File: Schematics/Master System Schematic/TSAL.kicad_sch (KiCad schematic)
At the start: 0 parts

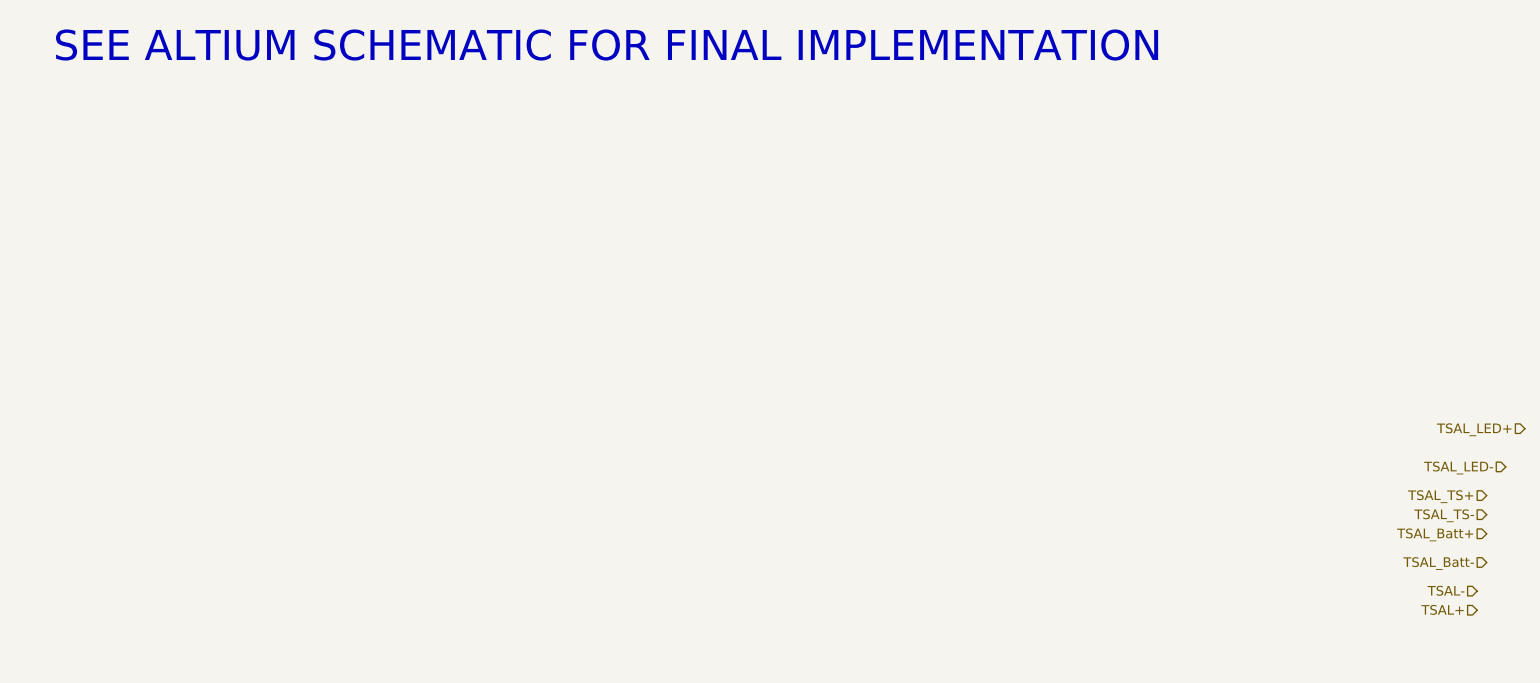
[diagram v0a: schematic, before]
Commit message: Clean up
- Cleaned TSAL
- Added some wire sizes to LV plate @ziptol you need to add remaining wire sizes here
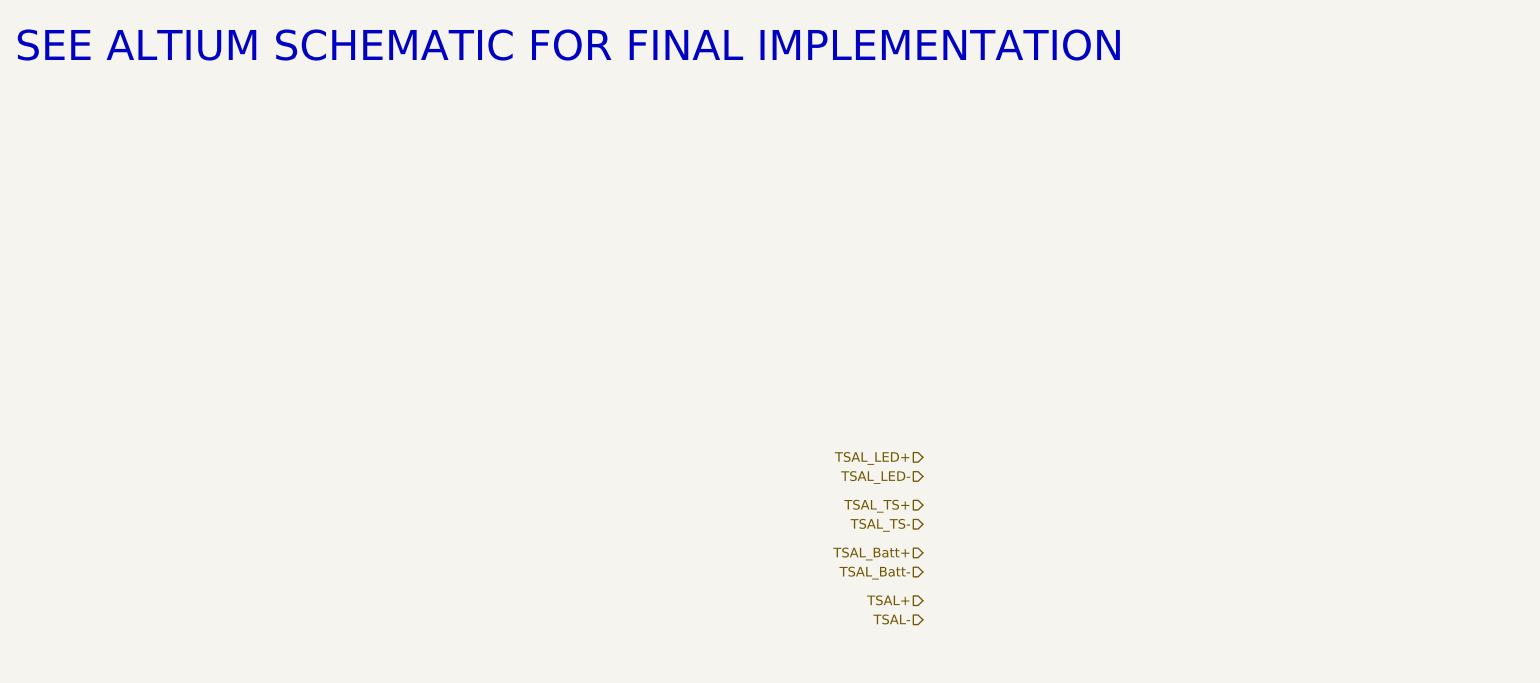
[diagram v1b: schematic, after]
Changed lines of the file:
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@@
 (kicad_sch (version 20211123) (generator eeschema)
-  (paper "A4")
+  (paper "A")
   (title_block
-    (date "2021-11-10")
+    (date "2022-01-29")
+    (rev "0")
     (company "Northeastern Electric Racing")
     (comment 1 "https://github.com/Northeastern-Electric-Racing/NER")
     (comment 2 "For authors and other info, contact Chief Electrical Engineer")
   )
-  (text "SEE ALTIUM SCHEMATIC FOR FINAL IMPLEMENTATION" (at 67.31 33.02 0)
+  (text "SEE ALTIUM SCHEMATIC FOR FINAL IMPLEMENTATION" (at 62.23 33.02 0)
     (effects (font (size 3.9878 3.9878)) (justify left bottom))
   )
-  (hierarchical_label "TSAL-" (shape input) (at 256.54 102.87 180)
+  (hierarchical_label "TSAL-" (shape input) (at 182.88 106.68 180)
     (effects (font (size 1.27 1.27)) (justify right))
   )
-  (hierarchical_label "TSAL_TS-" (shape input) (at 257.81 92.71 180)
+  (hierarchical_label "TSAL_TS-" (shape input) (at 182.88 93.98 180)
     (effects (font (size 1.27 1.27)) (justify right))
   )
-  (hierarchical_label "TSAL_LED+" (shape input) (at 262.89 81.28 180)
+  (hierarchical_label "TSAL_LED+" (shape input) (at 182.88 85.09 180)
     (effects (font (size 1.27 1.27)) (justify right))
   )
-  (hierarchical_label "TSAL_Batt-" (shape input) (at 257.81 99.06 180)
+  (hierarchical_label "TSAL_Batt-" (shape input) (at 182.88 100.33 180)
     (effects (font (size 1.27 1.27)) (justify right))
   )
-  (hierarchical_label "TSAL+" (shape input) (at 256.54 105.41 180)
+  (hierarchical_label "TSAL+" (shape input) (at 182.88 104.14 180)
     (effects (font (size 1.27 1.27)) (justify right))
   )
-  (hierarchical_label "TSAL_LED-" (shape input) (at 260.35 86.36 180)
+  (hierarchical_label "TSAL_LED-" (shape input) (at 182.88 87.63 180)
     (effects (font (size 1.27 1.27)) (justify right))
   )
-  (hierarchical_label "TSAL_Batt+" (shape input) (at 257.81 95.25 180)
+  (hierarchical_label "TSAL_Batt+" (shape input) (at 182.88 97.79 180)
     (effects (font (size 1.27 1.27)) (justify right))
   )
-  (hierarchical_label "TSAL_TS+" (shape input) (at 257.81 90.17 180)
+  (hierarchical_label "TSAL_TS+" (shape input) (at 182.88 91.44 180)
     (effects (font (size 1.27 1.27)) (justify right))
   )

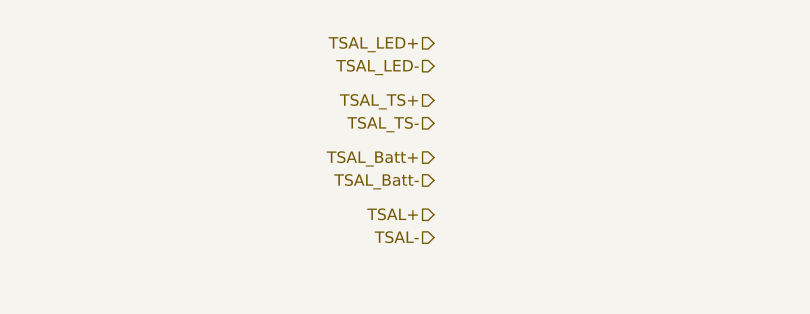
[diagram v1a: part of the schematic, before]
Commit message: Did a whole bunch of wire gauges and misc
Cleaned up runs
assigned wire gauges
implemented new glv/shutdown BRB placement design
updated some things in LV plate
started making names consistent
added new charger functionality in connector
left notes on some things to do
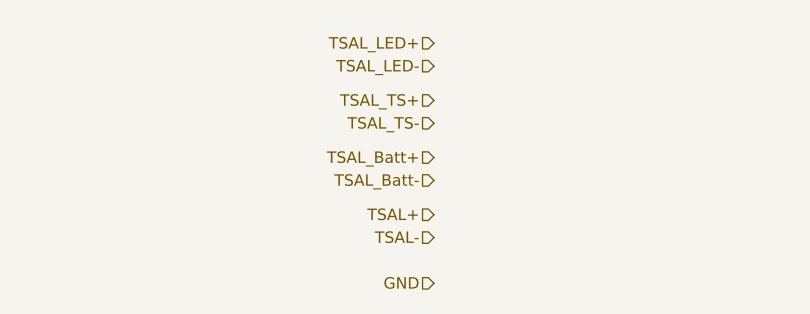
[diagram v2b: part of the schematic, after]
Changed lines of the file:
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@@
+    (effects (font (size 1.27 1.27)) (justify right))
+  )
+  (hierarchical_label "GND" (shape input) (at 182.88 111.76 180)
     (effects (font (size 1.27 1.27)) (justify right))
   )
